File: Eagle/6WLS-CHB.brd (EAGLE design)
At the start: 381.3 x 87 mm, 26 parts, among them U1 DCDCCHB7505, U2 DCDCCHB7515, U3 DCDCCHB7515

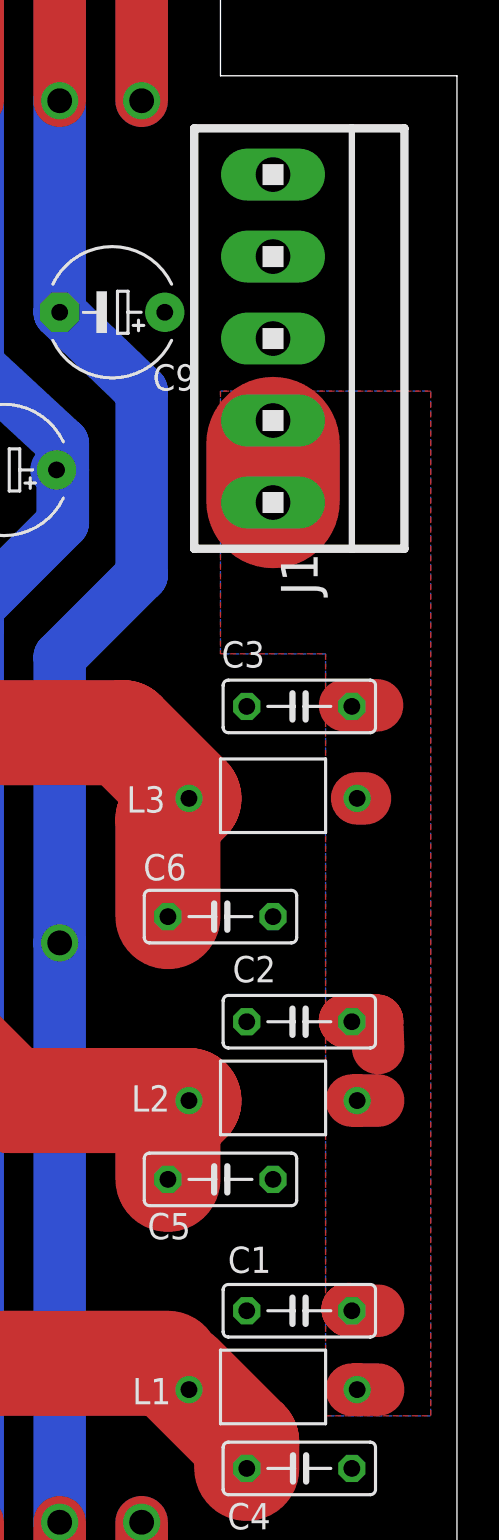
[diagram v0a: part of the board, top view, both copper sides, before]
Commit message: Bigger terminal block.
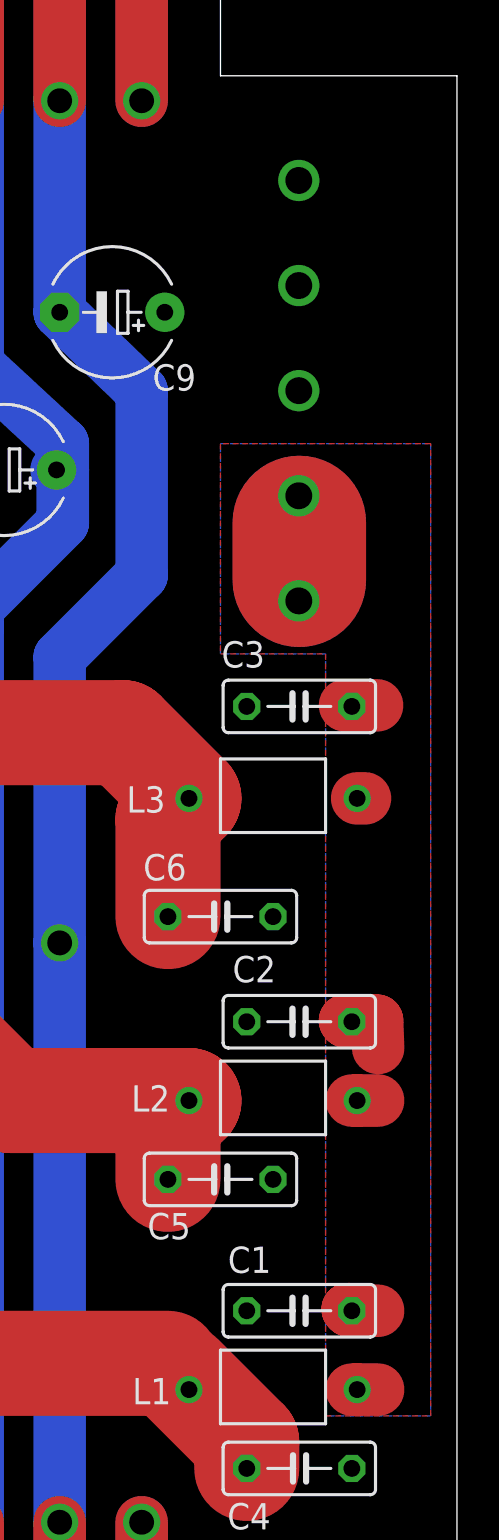
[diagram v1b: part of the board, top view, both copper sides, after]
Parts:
- removed J1: (no value), con-amp:1X5MTA
- added X1: MKDSN1,5/5-5,08, con-phoenix-508:MKDSN1,5/5-5,08
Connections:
- net 12V+: now also X1.4, X1.5
- net GND: now also X1.1, X1.2, X1.3
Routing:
- net 12V+: track 782.3 -> 790.3 mm
- net GND: track 25.6 -> 26.8 mm
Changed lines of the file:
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@@
 <text x="16.4973" y="26.924" size="1.27" layer="26" font="vector" ratio="12" rot="MR90">SCL</text>
 <text x="12.3825" y="22.733" size="1.27" layer="26" font="vector" ratio="12" rot="MR90">SDA</text>
-<text x="370.078" y="64.0842" size="1.27" layer="26" font="vector" ratio="12" rot="MR270">GND</text>
+<text x="371.348" y="62.8142" size="1.27" layer="26" font="vector" ratio="12" rot="MR270">GND</text>
 <text x="241.2111" y="63.9318" size="1.27" layer="26" font="vector" ratio="12" rot="MR90">NGND</text>
 <text x="261.8867" y="3.7084" size="1.27" layer="26" font="vector" ratio="12" rot="MR90">QGND</text>
@@
 <text x="182.88" y="8.8265" size="1.778" layer="25" font="vector" ratio="12">CINCON CHB50-12S15</text>
 <text x="86.36" y="8.8265" size="1.778" layer="25" font="vector" ratio="12">CINCON CHB50-12S15</text>
-<wire x1="368.554" y1="56.515" x2="370.586" y2="56.515" width="0.4064" layer="22"/>
-<text x="370.078" y="53.848" size="1.27" layer="26" font="vector" ratio="12" rot="MR270">12V</text>
+<wire x1="369.57" y1="53.34" x2="373.126" y2="53.34" width="0.4064" layer="22"/>
+<text x="371.348" y="52.578" size="1.27" layer="26" font="vector" ratio="12" rot="MR270">12V</text>
+<text x="371.348" y="67.8942" size="1.27" layer="26" font="vector" ratio="12" rot="MR270">GND</text>
+<text x="371.348" y="57.7342" size="1.27" layer="26" font="vector" ratio="12" rot="MR270">GND</text>
+<text x="371.348" y="47.498" size="1.27" layer="26" font="vector" ratio="12" rot="MR270">12V</text>
 </plain>
 <attributes>
@@
 </element>
 <element name="H15" library="holes" package="3,3-PAD" value="MOUNT-PAD-ROUND3.3" x="335.28" y="60.56"/>
-<element name="J1" library="con-amp" package="1X5MTA" value="" x="364.49" y="58.42" smashed="yes" rot="R270">
-<attribute name="NAME" x="364.871" y="48.0568" size="1.778" layer="25" rot="R270"/>
-<attribute name="VALUE" x="368.9408" y="67.8962" size="1.27" layer="27" rot="R270"/>
+<element name="X1" library="con-phoenix-508" package="MKDSN1,5/5-5,08" value="MKDSN1,5/5-5,08" x="365.76" y="55.88" smashed="yes" rot="MR270">
+<attribute name="NAME" x="361.315" y="68.2511" size="1.27" layer="26" font="vector" rot="MR270"/>
+<attribute name="VALUE" x="361.315" y="58.42" size="1.27" layer="28" font="vector" rot="MR270"/>
 </element>
 </elements>
@@
 <wire x1="29.21" y1="41.4528" x2="32.5628" y2="45.2628" width="1.27" layer="15"/>
 <via x="32.5628" y="45.2628" extent="1-16" drill="1.2"/>
-<wire x1="364.49" y1="53.34" x2="364.49" y2="50.546" width="6.4516" layer="1"/>
-<wire x1="364.49" y1="53.34" x2="364.49" y2="50.546" width="6.4516" layer="15"/>
 <polygon width="0.4064" layer="1">
-<vertex x="361.95" y="55.88"/>
+<vertex x="361.95" y="53.34"/>
 <vertex x="361.95" y="43.18"/>
 <vertex x="367.03" y="43.18"/>
 <vertex x="367.03" y="6.35"/>
 <vertex x="372.11" y="6.35"/>
-<vertex x="372.11" y="55.88"/>
+<vertex x="372.11" y="53.34"/>
 </polygon>
 <wire x1="367.9698" y1="40.6908" x2="369.5192" y2="40.6908" width="2.54" layer="1"/>
@@
 <wire x1="346.2528" y1="57.9628" x2="346.075" y2="57.785" width="1.778" layer="15"/>
 <polygon width="0.4064" layer="16">
-<vertex x="361.95" y="55.88"/>
-<vertex x="372.11" y="55.88"/>
+<vertex x="361.95" y="53.34"/>
+<vertex x="372.11" y="53.34"/>
 <vertex x="372.11" y="6.35"/>
 <vertex x="367.03" y="6.35"/>
@@
 </polygon>
 <wire x1="347.98" y1="55.88" x2="356.87" y2="55.88" width="1.778" layer="15"/>
-<wire x1="356.87" y1="55.88" x2="358.14" y2="54.61" width="1.778" layer="15"/>
-<wire x1="364.49" y1="53.34" x2="364.49" y2="53.34" width="0" layer="19" extent="1-15"/>
-<wire x1="366.8776" y1="54.61" x2="364.49" y2="53.34" width="0" layer="19" extent="1-15"/>
-<wire x1="367.9698" y1="40.6908" x2="364.49" y2="50.546" width="0" layer="19" extent="1-1"/>
-<wire x1="368.3" y1="40.64" x2="367.9698" y2="40.6908" width="0" layer="19" extent="1-1"/>
-<wire x1="368.554" y1="36.195" x2="368.3" y2="40.64" width="0" layer="19" extent="1-1"/>
-<wire x1="367.9698" y1="25.4508" x2="368.554" y2="36.195" width="0" layer="19" extent="1-1"/>
-<wire x1="369.57" y1="21.59" x2="369.57" y2="24.13" width="0" layer="19" extent="1-1"/>
-<wire x1="368.0968" y1="11.5062" x2="368.3" y2="21.59" width="0" layer="19" extent="1-1"/>
-<wire x1="368.3" y1="7.62" x2="368.3" y2="11.43" width="0" layer="19" extent="1-1"/>
-<wire x1="358.14" y1="54.61" x2="364.49" y2="54.61" width="1.778" layer="15"/>
-<wire x1="364.49" y1="54.61" x2="364.49" y2="53.34" width="0" layer="19" extent="1-16"/>
+<contactref element="X1" pad="4"/>
+<contactref element="X1" pad="5"/>
+<wire x1="356.87" y1="55.88" x2="361.95" y2="50.8" width="1.778" layer="15"/>
+<wire x1="361.95" y1="50.8" x2="365.7139" y2="50.8" width="1.778" layer="15"/>
+<wire x1="365.7139" y1="50.8" x2="365.735" y2="50.8211" width="1.778" layer="15"/>
+<wire x1="365.76" y1="49.53" x2="365.76" y2="46.736" width="6.4516" layer="1"/>
+<wire x1="365.76" y1="50.8" x2="365.76" y2="45.7661" width="1.778" layer="15"/>
+<wire x1="365.76" y1="45.7661" x2="365.735" y2="45.7411" width="1.778" layer="15"/>
+<wire x1="365.76" y1="49.53" x2="365.76" y2="46.736" width="6.4516" layer="16"/>
 </signal>
 <signal name="NC">
@@
 <wire x1="219.71" y1="45.72" x2="220.726" y2="45.72" width="2.54" layer="2"/>
 <wire x1="317.754" y1="45.72" x2="316.23" y2="45.72" width="2.54" layer="2"/>
-<wire x1="364.49" y1="59.69" x2="364.49" y2="66.04" width="6.4516" layer="2"/>
+<wire x1="365.76" y1="57.15" x2="365.76" y2="64.77" width="6.4516" layer="2"/>
 <wire x1="359.4354" y1="59.7154" x2="359.4608" y2="59.7154" width="2.54" layer="2"/>
 <wire x1="349.2754" y1="52.0954" x2="349.3008" y2="52.0954" width="2.54" layer="2"/>
 <wire x1="337.185" y1="54.61" x2="337.2104" y2="54.61" width="2.54" layer="2"/>
+<contactref element="X1" pad="1"/>
+<contactref element="X1" pad="2"/>
+<contactref element="X1" pad="3"/>
 <wire x1="261.5946" y1="1.1938" x2="241.808" y2="1.1938" width="0" layer="19" extent="2-2"/>
 <wire x1="267.97" y1="45.72" x2="261.62" y2="1.1938" width="0" layer="19" extent="2-2"/>
-<wire x1="359.4608" y1="59.7154" x2="364.49" y2="59.69" width="0" layer="19" extent="2-2"/>
+<wire x1="359.4354" y1="59.7154" x2="365.735" y2="60.9811" width="0" layer="19" extent="1-2"/>
+<wire x1="358.1908" y1="69.8754" x2="365.735" y2="66.0611" width="0" layer="19" extent="1-2"/>
 <wire x1="338.328" y1="69.85" x2="335.28" y2="61.214" width="0" layer="19" extent="2-2"/>
-<wire x1="358.1908" y1="69.8754" x2="364.49" y2="66.04" width="0" layer="19" extent="2-2"/>
 <wire x1="172.72" y1="55.88" x2="172.72" y2="45.72" width="0" layer="19" extent="2-2"/>
 <wire x1="123.19" y1="45.72" x2="123.19" y2="55.88" width="0" layer="19" extent="1-2"/>
@@
 <signal name="NC4">
 </signal>
-<signal name="N$4">
-<wire x1="377.19" y1="68.58" x2="383.6924" y2="68.58" width="0" layer="19" extent="1-16"/>
-</signal>
 </signals>
